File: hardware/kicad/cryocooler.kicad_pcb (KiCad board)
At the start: 4 copper layers, 130 x 110 mm, 291 parts, among them J1 USB_C, J10 RTD PT1000 4-wire, J11 AMP OUT (+ / -), J12 CRYOCOOLER (+ / -), J13 COMPRESSOR RELAY / GND, J14 IMU LSM6DSOX module, J2 12V IN, J3 FAN (4-pin PWM), J4 PUMP (4-pin PWM), J5 ALPHACOOL ES FLOW (3-pin), J6 ALPHACOOL ES NTC 10k, J7 PANEL BUTTON, J8 AMP REM / GND, J9 AMP SIGNAL IN / GND, Q1 IRF4905S, Q2 BSS138, Q3 BSS138, Q4 BSS138, Q5 BSS138, Q6 BSS84, Q7 BSS138, Q8 BSS84, SW1 RESET, SW2 BOOT, SW3 POWER, U1 ESP32-S3-WROOM-2-N32R16V, U10 EMC2303-x-KP, U11 LTC2954CTS8-2, U12 LM4040DBZ-5, U13 CL25N8-G, U14 ADS1220IPW, U15 AP63205WU-7, U16 LD1117S33TR, U17 ISO7741DW, U18 ACS37800KMACTR-030B3-SPI, U2 USBLC6-2SC6, U20 ADP5071AREZ, U21 ADP7142AUJZ, U22 ADP7182AUJZ, U23 INA239AIDGSR, U24 74AHCT1G125, U25 SC18IS604PW, U26 74LVC1G125, U3 SG-8002CA-PH 25MHz, U4 AD9833BRMZ, U5 OPA1656ID, U6 AD633JRZ-R7, U7 MCP4921-E/SN, U8 LM4040DBZ-2.5, U9 OPA188ID

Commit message: Add per-section supply jumpers, 8-pin IMU header and connector pin labels
- Four 1.27 mm 2-pin jumpers (JP1-JP4), each with a rail-on LED, cut the
  supply of one section for debugging: signal generator +3V3, +-15V
  generator +5V in, isolated amp-current supply +5V in, and a shared
  +3V3 net for the cooling chips (EMC2303, RTD ADC, I2C bridge).
- J14 is now an 8-pin JST XH in the Adafruit LSM6DSOX pad order
  (VIN, GND, SCL, SDA, DO, CS, I1, I2); firmware pin comments updated.
- Pin-function labels beside every connector, "RAILS ±15V" box title.
- Board re-placed and re-routed (130 x 110 mm); DRC 0 errors, 0 unconnected,
  ERC 0, 173 datasheet rules pass. BOM, READMEs, Gerbers and renders
  regenerated; link_usb_vbus.py now adapts to the routed layout.

Co-Authored-By: Claude Sonnet 5.5 <noreply@anthropic.com>
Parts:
- added D18: SIGNAL GEN +3V3 (green), LED_0603_1608Metric, F.Cu at (41.5, 17.8)
- added D19: +-15V SUPPLY +5V IN (green), LED_0603_1608Metric, F.Cu at (60.6, 78.4)
- added D20: ISOLATED SUPPLY +5V IN (green), LED_0603_1608Metric, F.Cu at (46.0, 61.6)
- added D21: COOLING +3V3 (EMC2303, RTD ADC, I2C BRIDGE) (green), LED_0603_1608Metric, F.Cu at (88.3, 92.3)
- added JP1: EN SG3, PinHeader_1x02_P1.27mm_Vertical, F.Cu at (49.0, 15.6)
- added JP2: EN PS15, PinHeader_1x02_P1.27mm_Vertical, F.Cu at (56.0, 79.0)
- added JP3: EN ISO5, PinHeader_1x02_P1.27mm_Vertical, F.Cu at (43.6, 52.6)
- added JP4: EN COOL, PinHeader_1x02_P1.27mm_Vertical, F.Cu at (106.9, 80.6)
- added R96: 1k, R_0603_1608Metric, F.Cu at (44.5, 17.6)
- added R97: 1k, R_0603_1608Metric, F.Cu at (64.5, 76.4)
- added R98: 1k, R_0603_1608Metric, F.Cu at (45.1, 58.6)
- added R99: 1k, R_0603_1608Metric, F.Cu at (90.6, 89.3)
- J14: footprint JST_XH_B10B-XH-A_1x10_P2.50mm_Vertical -> JST_XH_B8B-XH-A_1x08_P2.50mm_Vertical
- moved C73 41.8 mm to (40.1, 76.5)
- moved C41 35.0 mm to (42.9, 85.3), turned to -90 degrees
- moved C43 32.0 mm to (29.9, 93.0)
- moved C40 26.7 mm to (46.9, 90.5), turned to 180 degrees
- moved C74 26.3 mm to (25.6, 95.5)
- moved TP36 25.0 mm to (104.8, 31.2)
- moved TP17 24.8 mm to (35.4, 64.1)
- moved C52 24.1 mm to (25.9, 39.9), turned to 180 degrees
- moved R44 23.7 mm to (126.0, 73.8), turned to 0 degrees
- moved TP41 22.8 mm to (39.1, 13.4)
- moved J14 22.5 mm to (119.4, 45.7), turned to -90 degrees
- moved R94 21.3 mm to (122.4, 67.7), turned to 180 degrees
- moved C42 18.7 mm to (50.6, 83.2)
- moved C56 16.5 mm to (55.5, 55.9), turned to -90 degrees
- moved C57 16.4 mm to (70.5, 62.2)
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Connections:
- C20 pad 1: +3V3 -> +3V3_SG
- C21 pad 1: +3V3 -> +3V3_SG
- C24 pad 1: +3V3 -> +3V3_COOL
- C25 pad 1: +3V3 -> +3V3_COOL
- C31 pad 1: +3V3 -> +3V3_COOL
- C32 pad 1: +3V3 -> +3V3_COOL
- C45 pad 1: +5V -> +5V_ISO
- C46 pad 1: +5V -> +5V_ISO
- C56 pad 1: +5V -> +5V_PS15
- C57 pad 1: +5V -> +5V_PS15
- C58 pad 1: +5V -> +5V_PS15
- C77 pad 1: +3V3 -> +3V3_COOL
- C78 pad 1: +3V3 -> +3V3_COOL
- C79 pad 1: +3V3 -> +3V3_COOL
- J14 pad 4: GND -> Net-(J14-Pin_4)
- J14 pad 7: GND -> Net-(J14-Pin_7)
- PS1 pad 9_10: +5V -> +5V_ISO
- R11 pad 1: +3V3 -> +3V3_SG
- R48 pad 1: +5V -> +5V_ISO
- R91 pad 2: Net-(J14-Pin_5) -> Net-(J14-Pin_4)
- R92 pad 2: Net-(J14-Pin_6) -> Net-(J14-Pin_5)
- R93 pad 2: Net-(J14-Pin_8) -> Net-(J14-Pin_6)
- R94 pad 2: Net-(J14-Pin_9) -> Net-(J14-Pin_7)
- R95 pad 2: Net-(J14-Pin_10) -> Net-(J14-Pin_8)
- U10 pad 3: +3V3 -> +3V3_COOL
- U14 pad 12: +3V3 -> +3V3_COOL
- U14 pad 13: +3V3 -> +3V3_COOL
- U20 pad 11: +5V -> +5V_PS15
- U20 pad 17: +5V -> +5V_PS15
- U20 pad 18: +5V -> +5V_PS15
- U20 pad 19: +5V -> +5V_PS15
- U20 pad 9: +5V -> +5V_PS15
- U25 pad 12: +3V3 -> +3V3_COOL
- U25 pad 15: +3V3 -> +3V3_COOL
- U26 pad 5: +3V3 -> +3V3_COOL
- U7 pad 1: +3V3 -> +3V3_SG
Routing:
- net +3V3_COOL: track 0.00 -> 84.6 mm, vias 0 -> 3
- net +5V_PS15: track 0.00 -> 75.2 mm, vias 0 -> 1
- net +3V3: track 572.0 -> 507.3 mm, vias 10 -> 14
- net +3V3_SG: track 0.00 -> 33.8 mm, vias 0 -> 3
- net ISO_3V3: track 65.7 -> 95.6 mm, vias 0 -> 2
- net +5V_ISO: track 0.00 -> 28.9 mm
- net +5V: track 341.4 -> 313.0 mm, vias 5 -> 3
- net SIG_SINE: track 21.4 -> 43.2 mm
- net IMU_INT1: track 29.8 -> 47.1 mm, vias 0 -> 3
- net Net-(J14-Pin_7): track 0.00 -> 17.3 mm, vias 0 -> 1
- net GND: track 492.7 -> 509.6 mm, vias 193 -> 158
- net FLOW_TACH: track 118.4 -> 101.9 mm, vias 3 -> 2
- net Net-(U6-X1): track 21.7 -> 6.16 mm, vias 3 -> 0
- net +12V: track 326.7 -> 312.3 mm
- net MCP4921_CS: track 93.5 -> 80.4 mm, vias 3 -> 2
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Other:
- board text added: "+"
- board text added: "+12V"
- board text added: "-"
- board text added: "BTN"
- board text added: "COOL 3V3"
- board text added: "CS"
- board text added: "DO"
- board text added: "F+"
- board text added: "F-"
- board text added: "GND"
- board text added: "I1"
- board text added: "I2"
- board text added: "ISO PS"
- board text added: "NTC"
- board text added: "PANEL"
- board text added: "PWM"
- board text added: "RAILS ±15V"
- board text added: "REM"
- board text added: "S+"
- board text added: "S-"
- board text added: "SCL"
- board text added: "SDA"
- board text added: "SG 3V3"
- board text added: "SIG"
- board text added: "TACH"
- board text added: "VIN"
- board text added: "±15 PS"
- board text removed: "PANEL BTN"
- board text removed: "RAILS +-15V"

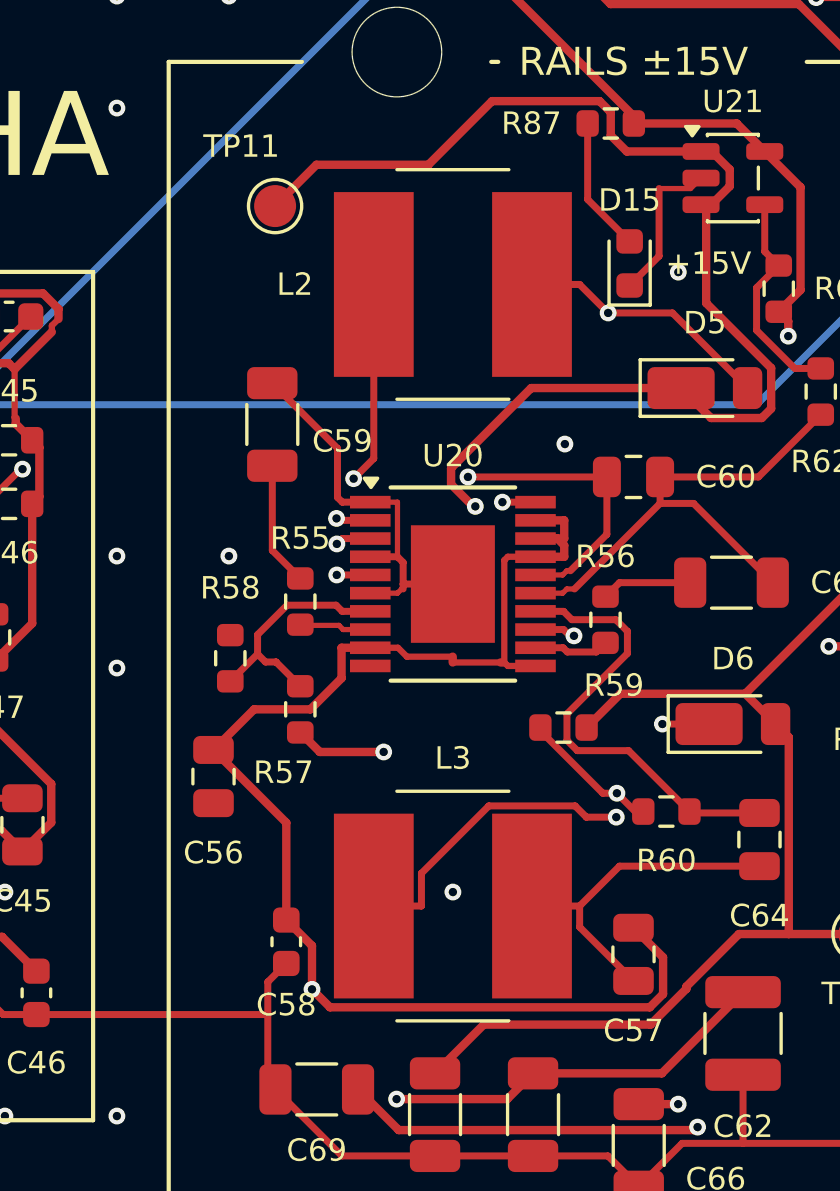
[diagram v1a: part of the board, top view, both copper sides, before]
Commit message: Swap L2/L3 for shielded Bourns SRP7050TA inductors
L2 (3.3 uH boost) and L3 (6.8 uH inverting) were semi-shielded SRN8040TA
parts. Replace them with fully shielded SRP7050TA-3R3M / -6R8M, using a
new L_Bourns_SRP7050TA footprint (datasheet land pattern, 7.3 x 6.6 mm
body) and a 5.0 mm envelope model. The routed board keeps its tracks (the
footprints were swapped in place and the pours refilled); DRC 0 errors,
0 unconnected. Gerbers and BOM regenerated.

Co-Authored-By: Claude Sonnet 5.5 <noreply@anthropic.com>
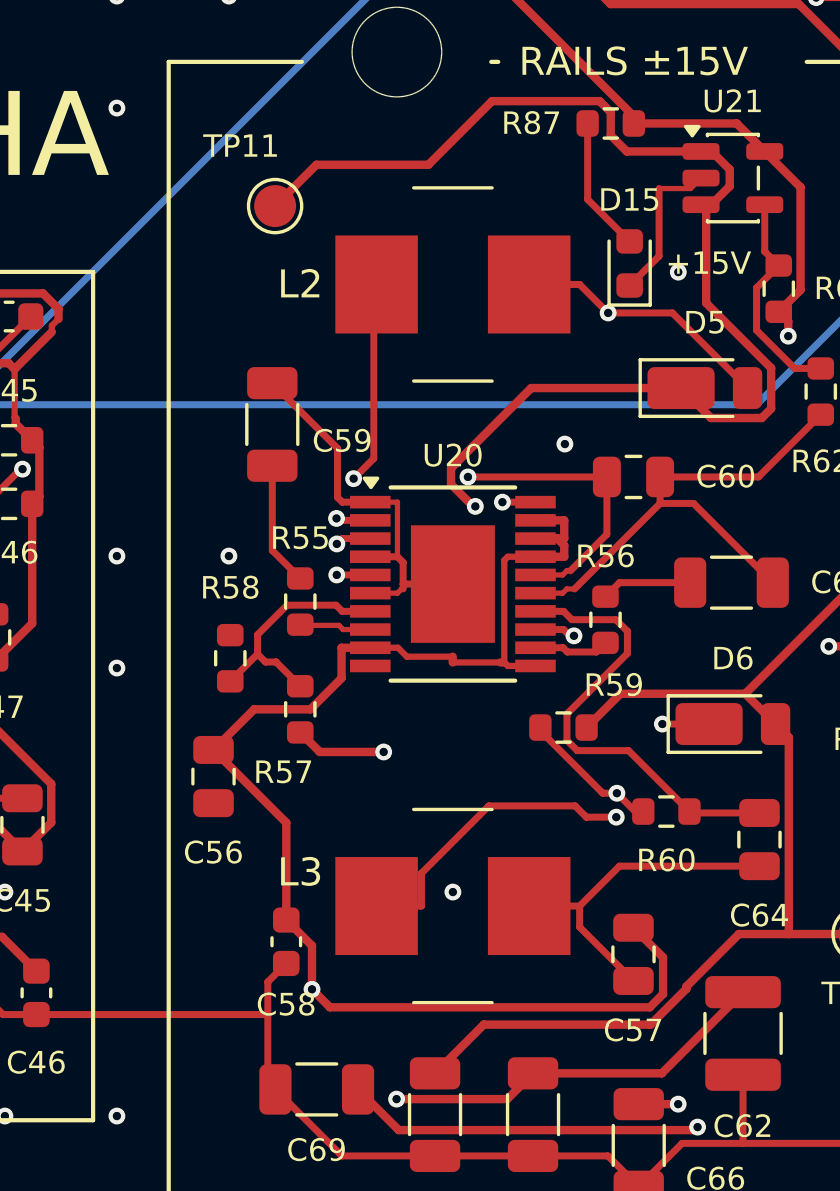
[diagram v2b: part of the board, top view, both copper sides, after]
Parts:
- L2: value SRN8040TA-3R3M -> SRP7050TA-3R3M; footprint L_Bourns_SRN8040TA -> L_Bourns_SRP7050TA
- L3: value SRN8040TA-6R8M -> SRP7050TA-6R8M; footprint L_Bourns_SRN8040TA -> L_Bourns_SRP7050TA

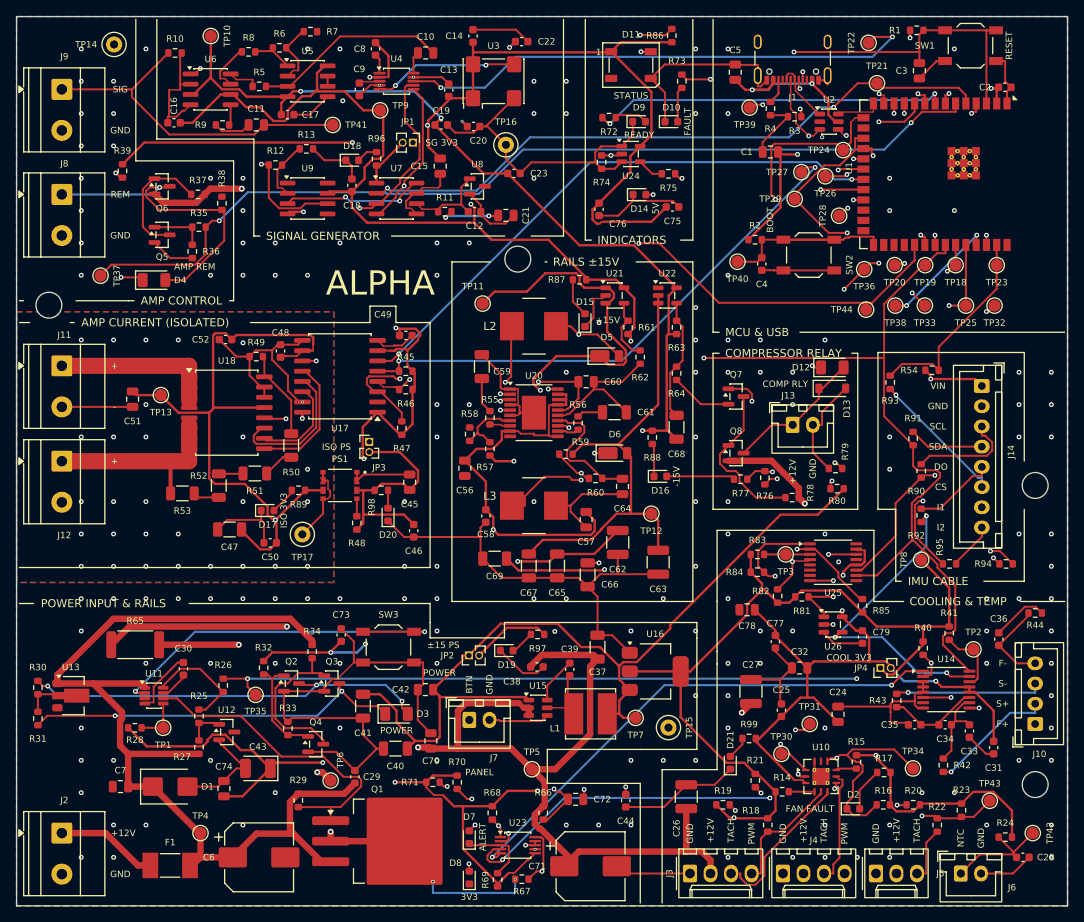
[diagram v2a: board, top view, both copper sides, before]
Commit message: Split cooling into Water Cooling and Cold Head Temp sections, each with a supply jumper and LED
Water Cooling (EMC2303, SC18IS604 bridge, NTC, fan/pump/flow) sits behind JP4
on +3V3_COOL together with its pull-ups. Cold Head Temp (ADS1220, PT1000) gets
a new jumper JP5 and LED D22 on +3V3_CH. JP2 is relabelled for the +-15V rails
and moved into the RAILS +-15V box. PCB regenerated with two silk boxes, routed,
leftovers finished with a grid router; board render added to the main README.

Co-Authored-By: Claude Sonnet 5.5 <noreply@anthropic.com>
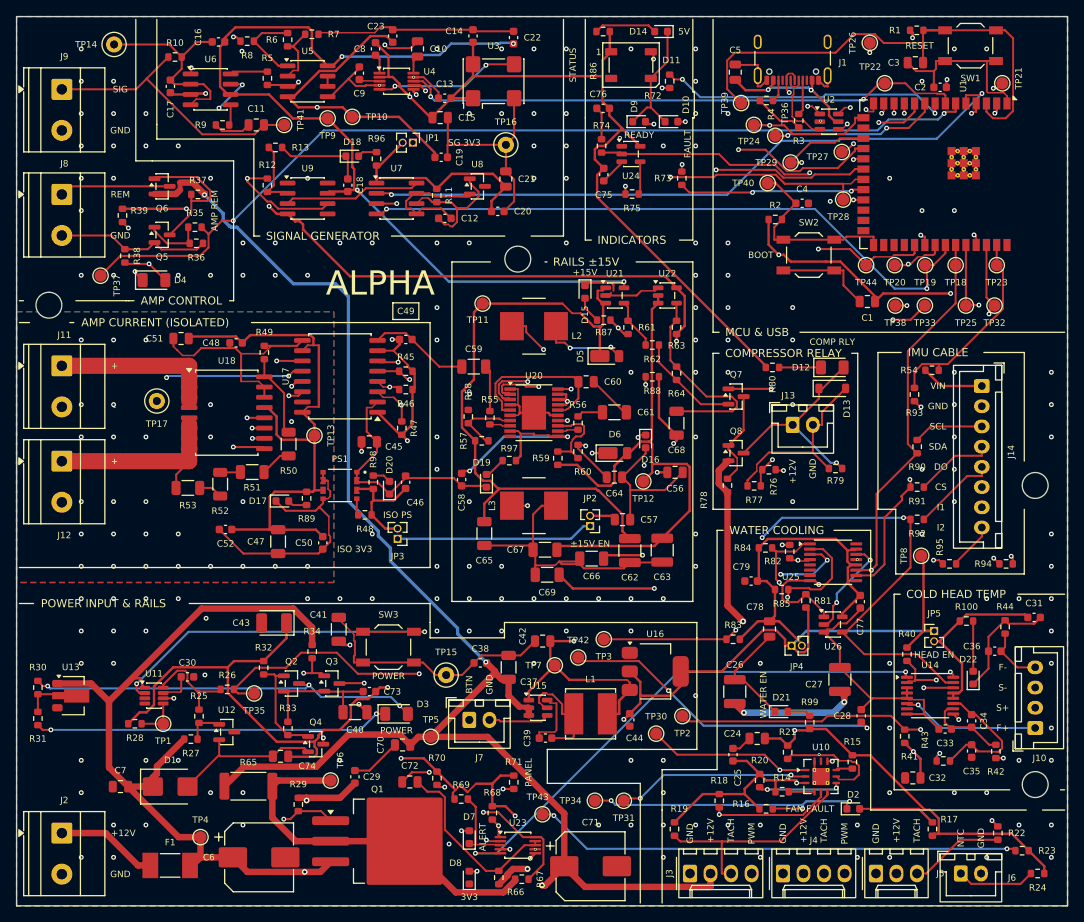
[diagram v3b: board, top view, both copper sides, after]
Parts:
- added D22: COLD HEAD +3V3 (ADS1220 RTD ADC) (green), LED_0603_1608Metric, F.Cu at (118.3, 81.8)
- added JP5: EN CH, PinHeader_1x02_P1.27mm_Vertical, F.Cu at (113.5, 76.0)
- added R100: 1k, R_0603_1608Metric, F.Cu at (117.5, 74.8)
- D19: value +-15V SUPPLY +5V IN (green) -> +-15V RAILS ENABLE (+5V IN) (green)
- D21: value COOLING +3V3 (EMC2303, RTD ADC, I2C BRIDGE) (green) -> WATER COOLING +3V3 (EMC2303, I2C BRIDGE, NTC) (green)
- moved TP42 60.3 mm to (69.5, 79.3)
- moved TP43 55.4 mm to (65.1, 98.7)
- moved TP34 39.6 mm to (71.5, 97.0)
- moved TP2 36.9 mm to (82.4, 86.5)
- moved TP15 28.3 mm to (53.1, 81.5)
- moved C28 26.6 mm to (104.5, 86.5), turned to 90 degrees
- moved C56 26.0 mm to (81.5, 56.4), turned to 0 degrees
- moved TP31 24.9 mm to (75.1, 97.0)
- moved TP3 24.8 mm to (72.6, 77.0)
- moved TP17 24.4 mm to (17.4, 47.6)
- moved C52 23.5 mm to (25.9, 63.4)
- moved C23 22.7 mm to (46.5, 2.40), turned to 90 degrees
- moved R65 22.4 mm to (28.7, 95.2)
- moved C1 22.1 mm to (105.2, 35.2)
- moved JP2 21.9 mm to (71.0, 63.0), turned to 180 degrees
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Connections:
- net /I2C Bridge/BRIDGE_INT renamed /Water Cooling I2C Bridge/BRIDGE_INT
- C31 pad 1: +3V3_COOL -> +3V3_CH
- C32 pad 1: +3V3_COOL -> +3V3_CH
- R14 pad 1: +3V3 -> +3V3_COOL
- R15 pad 1: +3V3 -> +3V3_COOL
- R16 pad 1: +3V3 -> +3V3_COOL
- R17 pad 1: +3V3 -> +3V3_COOL
- R18 pad 1: +3V3 -> +3V3_COOL
- R19 pad 1: +3V3 -> +3V3_COOL
- R20 pad 1: +3V3 -> +3V3_COOL
- R21 pad 1: +3V3 -> +3V3_COOL
- R23 pad 1: +3V3 -> +3V3_COOL
- R24 pad 1: +3V3 -> +3V3_COOL
- R41 pad 1: +3V3 -> +3V3_CH
- R83 pad 1: +3V3 -> +3V3_COOL
- R84 pad 1: +3V3 -> +3V3_COOL
- R85 pad 1: +3V3 -> +3V3_COOL
- U14 pad 12: +3V3_COOL -> +3V3_CH
- U14 pad 13: +3V3_COOL -> +3V3_CH
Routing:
- net +3V3: track 507.3 -> 414.1 mm, vias 14 -> 13
- net FLOW_TACH: track 101.9 -> 179.8 mm, vias 2 -> 4
- net +3V3_COOL: track 84.6 -> 136.3 mm, vias 3 -> 2
- net NTC_ADC: track 113.0 -> 156.1 mm, vias 1 -> 3
- net +3V3_CH: track 0.00 -> 42.0 mm, vias 0 -> 1
- net Net-(U14-~{DRDY}): track 8.50 -> 39.7 mm, vias 0 -> 2
- net -15V: track 154.4 -> 184.8 mm, vias 5 -> 6
- net +5V: track 313.0 -> 283.6 mm, vias 3 -> 5
- net /Water Cooling I2C Bridge/BRIDGE_INT: track 5.67 -> 34.9 mm, vias 0 -> 3
- net GND: track 509.6 -> 535.6 mm, vias 158 -> 177
- net +12V: track 312.3 -> 287.1 mm, vias 5 -> 7
- net ISO_3V3: track 95.6 -> 71.5 mm, vias 2 -> 0
- net PWR_KILL: track 148.3 -> 127.6 mm, vias 3 -> 2
- net FAN_ALERT: track 96.7 -> 115.4 mm, vias 2 -> 5
- net Net-(D14-A): track 26.0 -> 7.84 mm, vias 2 -> 0
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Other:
- board text added: "COLD HEAD TEMP"
- board text added: "HEAD EN"
- board text added: "WATER COOLING"
- board text added: "WATER EN"
- board text added: "±15V EN"
- board text removed: "-15V"
- board text removed: "COOL 3V3"
- board text removed: "COOLING & TEMP"
- board text removed: "±15 PS"
